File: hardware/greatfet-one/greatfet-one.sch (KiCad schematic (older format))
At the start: 98 parts, among them J1 NEIGHBOR1, J2 NEIGHBOR2, J3 USB-MICRO-B-SHIELDED, J4 USB-MICRO-B-SHIELDED, J5 JTAG, J6 POWER, J7 BONUS_ROW, SW1 DFU, SW2 RESET, U1 LPC4330FBD144, U2 W25Q16DV, U3 AP7333, U4 IP4220CZ6, U5 AP2553W6-7, X1 MCU_XTAL, X2 RTC_XTAL

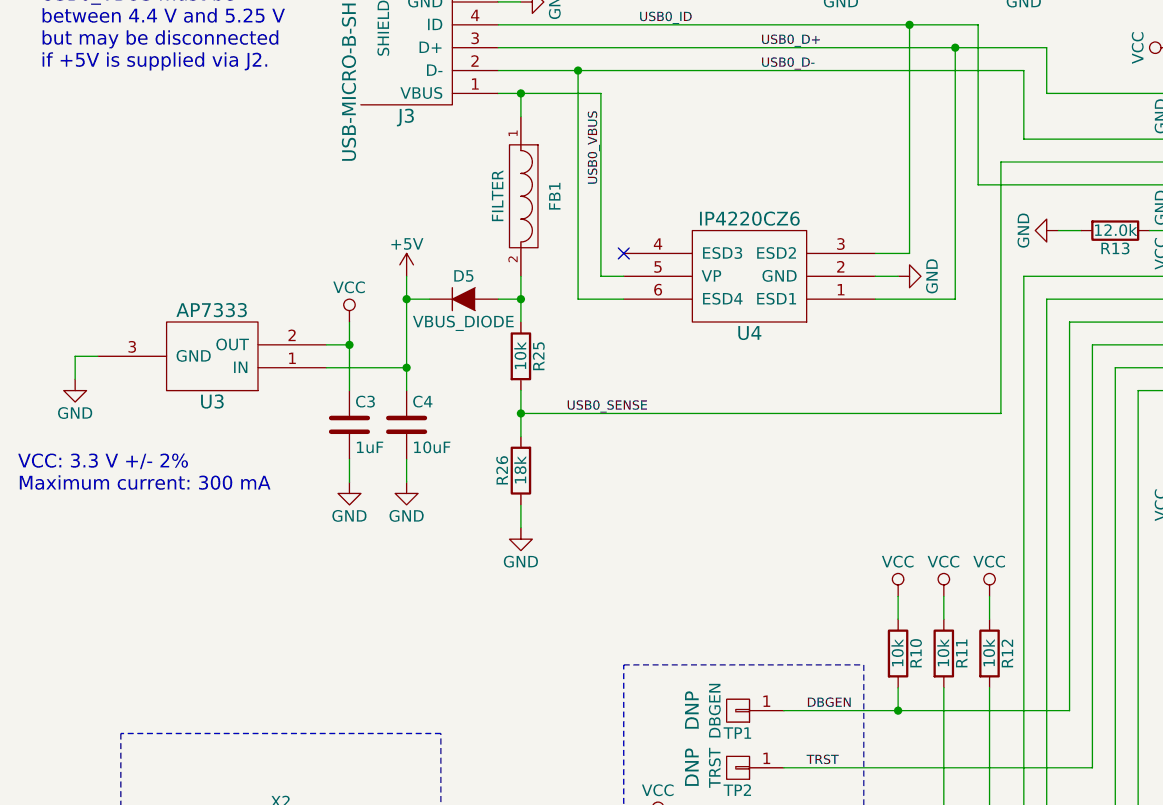
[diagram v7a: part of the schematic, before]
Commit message: GreatFET One: solder jumper to bypass VBUS diode
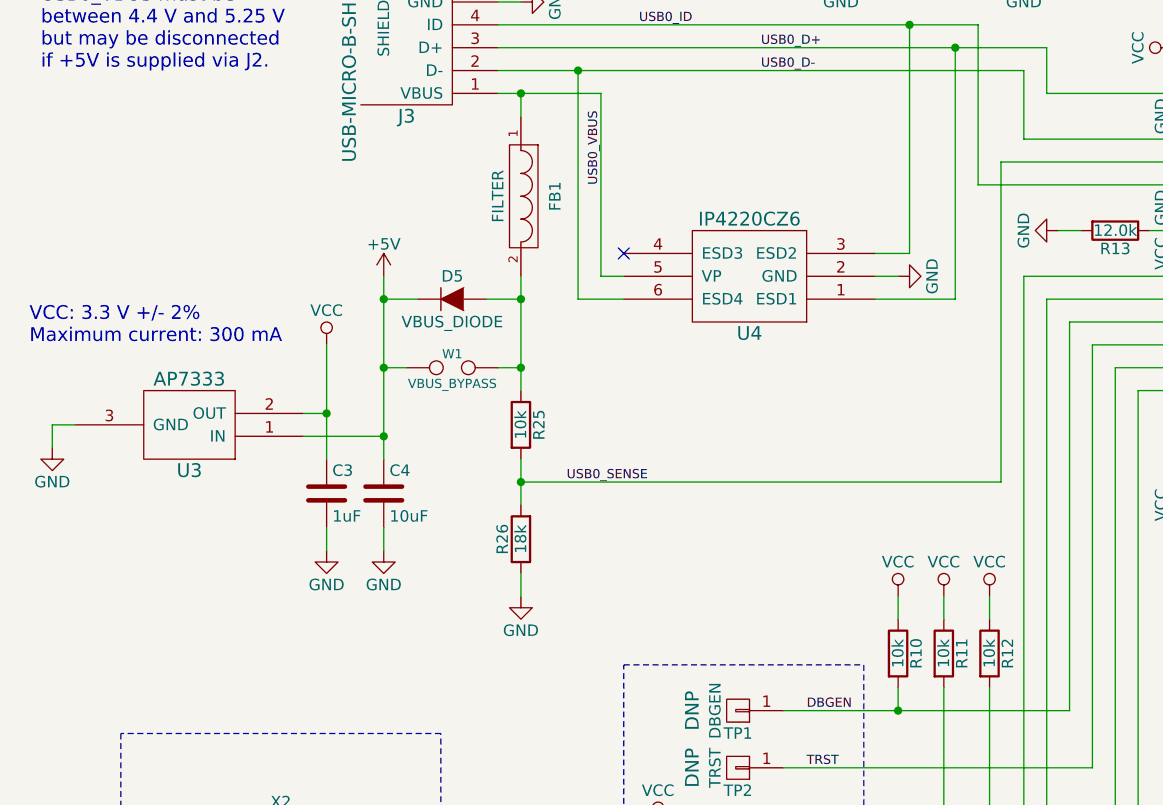
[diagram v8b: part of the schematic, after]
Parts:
- added W1: VBUS_BYPASS, gsg-modules:0603-JUMPER, symbol TEST
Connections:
- net +5V: now also W1.1
- net at D5.2 (A), FB1.2, R25.1: now also W1.2
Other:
- moved on the sheet: C3, C4, D5, R25, R26, U3
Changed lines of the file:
@@
 L AP7333 U3
 U 1 1 55E0B3C4
-P 1450 6450
-F 0 "U3" H 1450 6650 60  0000 C CNN
-F 1 "AP7333" H 1450 6250 60  0000 C CNN
-F 2 "gsg-modules:SOT23-3" H 1450 6450 60  0001 C CNN
-F 3 "" H 1450 6450 60  0000 C CNN
-F 4 "Diodes Inc." H 1450 6450 60  0001 C CNN "Manufacturer"
-F 5 "AP7333-33SAG-7" H 1450 6450 60  0001 C CNN "Part Number"
-F 6 "IC REG LDO 3.3V .3A SOT23" H 1450 6450 60  0001 C CNN "Description"
-	1    1450 6450
+P 1350 6750
+F 0 "U3" H 1350 6950 60  0000 C CNN
+F 1 "AP7333" H 1350 6550 60  0000 C CNN
+F 2 "gsg-modules:SOT23-3" H 1350 6750 60  0001 C CNN
+F 3 "" H 1350 6750 60  0000 C CNN
+F 4 "Diodes Inc." H 1350 6750 60  0001 C CNN "Manufacturer"
+F 5 "AP7333-33SAG-7" H 1350 6750 60  0001 C CNN "Part Number"
+F 6 "IC REG LDO 3.3V .3A SOT23" H 1350 6750 60  0001 C CNN "Description"
+	1    1350 6750
 	-1   0    0    1
 $EndComp
@@
 L C C4
 U 1 1 55E46B79
-P 2300 6750
-F 0 "C4" H 2325 6850 50  0000 L CNN
-F 1 "10uF" H 2325 6650 50  0000 L CNN
-F 2 "gsg-modules:0805" H 2338 6600 30  0001 C CNN
-F 3 "" H 2300 6750 60  0000 C CNN
-F 4 "Murata" H 2300 6750 60  0001 C CNN "Manufacturer"
-F 5 "GRM21BR61A106KE19L" H 2300 6750 60  0001 C CNN "Part Number"
-F 6 "CAP CER 10UF 10V 10% X5R 0805" H 2300 6750 60  0001 C CNN "Description"
-	1    2300 6750
+P 2200 7050
+F 0 "C4" H 2225 7150 50  0000 L CNN
+F 1 "10uF" H 2225 6950 50  0000 L CNN
+F 2 "gsg-modules:0805" H 2238 6900 30  0001 C CNN
+F 3 "" H 2200 7050 60  0000 C CNN
+F 4 "Murata" H 2200 7050 60  0001 C CNN "Manufacturer"
+F 5 "GRM21BR61A106KE19L" H 2200 7050 60  0001 C CNN "Part Number"
+F 6 "CAP CER 10UF 10V 10% X5R 0805" H 2200 7050 60  0001 C CNN "Description"
+	1    2200 7050
 	1    0    0    -1
 $EndComp
@@
 L C C3
 U 1 1 55E46D07
-P 2050 6750
-F 0 "C3" H 2075 6850 50  0000 L CNN
-F 1 "1uF" H 2075 6650 50  0000 L CNN
-F 2 "gsg-modules:0603" H 2088 6600 30  0001 C CNN
-F 3 "" H 2050 6750 60  0000 C CNN
-F 4 "Taiyo Yuden" H 2050 6750 60  0001 C CNN "Manufacturer"
-F 5 "LMK107B7105KA-T" H 2050 6750 60  0001 C CNN "Part Number"
-F 6 "CAP CER 1UF 10V 10% X7R 0603" H 2050 6750 60  0001 C CNN "Description"
-	1    2050 6750
+P 1950 7050
+F 0 "C3" H 1975 7150 50  0000 L CNN
+F 1 "1uF" H 1975 6950 50  0000 L CNN
+F 2 "gsg-modules:0603" H 1988 6900 30  0001 C CNN
+F 3 "" H 1950 7050 60  0000 C CNN
+F 4 "Taiyo Yuden" H 1950 7050 60  0001 C CNN "Manufacturer"
+F 5 "LMK107B7105KA-T" H 1950 7050 60  0001 C CNN "Part Number"
+F 6 "CAP CER 1UF 10V 10% X7R 0603" H 1950 7050 60  0001 C CNN "Description"
+	1    1950 7050
 	1    0    0    -1
 $EndComp
@@
 L VCC #PWR020
 U 1 1 55E4762F
-P 2050 6300
-F 0 "#PWR020" H 2050 6150 50  0001 C CNN
-F 1 "VCC" H 2050 6450 50  0000 C CNN
-F 2 "" H 2050 6300 60  0000 C CNN
-F 3 "" H 2050 6300 60  0000 C CNN
-	1    2050 6300
+P 1950 6400
+F 0 "#PWR020" H 1950 6250 50  0001 C CNN
+F 1 "VCC" H 1950 6550 50  0000 C CNN
+F 2 "" H 1950 6400 60  0000 C CNN
+F 3 "" H 1950 6400 60  0000 C CNN
+	1    1950 6400
 	1    0    0    -1
 $EndComp
@@
 L GND #PWR021
 U 1 1 55E47864
-P 2050 7000
-F 0 "#PWR021" H 2050 6750 50  0001 C CNN
-F 1 "GND" H 2050 6850 50  0000 C CNN
-F 2 "" H 2050 7000 60  0000 C CNN
-F 3 "" H 2050 7000 60  0000 C CNN
-	1    2050 7000
+P 1950 7300
+F 0 "#PWR021" H 1950 7050 50  0001 C CNN
+F 1 "GND" H 1950 7150 50  0000 C CNN
+F 2 "" H 1950 7300 60  0000 C CNN
+F 3 "" H 1950 7300 60  0000 C CNN
+	1    1950 7300
 	1    0    0    -1
 $EndComp
@@
 L GND #PWR022
 U 1 1 55E478D5
-P 2300 7000
-F 0 "#PWR022" H 2300 6750 50  0001 C CNN
-F 1 "GND" H 2300 6850 50  0000 C CNN
-F 2 "" H 2300 7000 60  0000 C CNN
-F 3 "" H 2300 7000 60  0000 C CNN
-	1    2300 7000
+P 2200 7300
+F 0 "#PWR022" H 2200 7050 50  0001 C CNN
+F 1 "GND" H 2200 7150 50  0000 C CNN
+F 2 "" H 2200 7300 60  0000 C CNN
+F 3 "" H 2200 7300 60  0000 C CNN
+	1    2200 7300
 	1    0    0    -1
 $EndComp
@@
 L GND #PWR023
 U 1 1 55E47A1E
-P 850 6550
-F 0 "#PWR023" H 850 6300 50  0001 C CNN
-F 1 "GND" H 850 6400 50  0000 C CNN
-F 2 "" H 850 6550 60  0000 C CNN
-F 3 "" H 850 6550 60  0000 C CNN
-	1    850  6550
+P 750 6850
+F 0 "#PWR023" H 750 6600 50  0001 C CNN
+F 1 "GND" H 750 6700 50  0000 C CNN
+F 2 "" H 750 6850 60  0000 C CNN
+F 3 "" H 750 6850 60  0000 C CNN
+	1    750  6850
 	1    0    0    -1
 $EndComp
@@
 Text Label 14050 6350 1    40   ~ 0
 USB1_SHIELD
-Text Notes 600  7050 0    60   ~ 0
+Text Notes 650  6400 0    60   ~ 0
 VCC: 3.3 V +/- 2%\nMaximum current: 300 mA
 $Comp
 L D D5
 U 1 1 57C0D534
-P 2550 6200
-F 0 "D5" H 2550 6300 50  0000 C CNN
-F 1 "VBUS_DIODE" H 2550 6100 50  0000 C CNN
-F 2 "gsg-modules:B140-13-F" H 2550 6200 60  0001 C CNN
-F 3 "" H 2550 6200 60  0000 C CNN
-F 4 "Diodes Inc." H 2550 6200 60  0001 C CNN "Manufacturer"
-F 5 "B140-13-F" H 2550 6200 60  0001 C CNN "Part Number"
-F 6 "DIODE SCHOTTKY 40V 1A SMA" H 2550 6200 60  0001 C CNN "Description"
-	1    2550 6200
+P 2500 6200
+F 0 "D5" H 2500 6300 50  0000 C CNN
+F 1 "VBUS_DIODE" H 2500 6100 50  0000 C CNN
+F 2 "gsg-modules:B140-13-F" H 2500 6200 60  0001 C CNN
+F 3 "" H 2500 6200 60  0000 C CNN
+F 4 "Diodes Inc." H 2500 6200 60  0001 C CNN "Manufacturer"
+F 5 "B140-13-F" H 2500 6200 60  0001 C CNN "Part Number"
+F 6 "DIODE SCHOTTKY 40V 1A SMA" H 2500 6200 60  0001 C CNN "Description"
+	1    2500 6200
 	1    0    0    -1
 $EndComp
@@
 L GND #PWR083
 U 1 1 57C0FA0A
-P 2800 7200
-F 0 "#PWR083" H 2800 6950 50  0001 C CNN
-F 1 "GND" H 2800 7050 50  0000 C CNN
-F 2 "" H 2800 7200 60  0000 C CNN
-F 3 "" H 2800 7200 60  0000 C CNN
-	1    2800 7200
+P 2800 7500
+F 0 "#PWR083" H 2800 7250 50  0001 C CNN
+F 1 "GND" H 2800 7350 50  0000 C CNN
+F 2 "" H 2800 7500 60  0000 C CNN
+F 3 "" H 2800 7500 60  0000 C CNN
+	1    2800 7500
 	1    0    0    -1
 $EndComp
@@
 L R R25
 U 1 1 57C0FA13
-P 2800 6450
-F 0 "R25" V 2880 6450 50  0000 C CNN
-F 1 "10k" V 2800 6450 50  0000 C CNN
-F 2 "gsg-modules:0603" V 2730 6450 30  0001 C CNN
-F 3 "" H 2800 6450 30  0000 C CNN
-F 4 "Panasonic" H 2800 6450 60  0001 C CNN "Manufacturer"
-F 5 "ERJ-3GEYJ103V" H 2800 6450 60  0001 C CNN "Part Number"
-F 6 "RES 10K OHM 1/10W 5% 0603 SMD" H 2800 6450 60  0001 C CNN "Description"
-	1    2800 6450
+P 2800 6750
+F 0 "R25" V 2880 6750 50  0000 C CNN
+F 1 "10k" V 2800 6750 50  0000 C CNN
+F 2 "gsg-modules:0603" V 2730 6750 30  0001 C CNN
+F 3 "" H 2800 6750 30  0000 C CNN
+F 4 "Panasonic" H 2800 6750 60  0001 C CNN "Manufacturer"
+F 5 "ERJ-3GEYJ103V" H 2800 6750 60  0001 C CNN "Part Number"
+F 6 "RES 10K OHM 1/10W 5% 0603 SMD" H 2800 6750 60  0001 C CNN "Description"
+	1    2800 6750
 	1    0    0    -1
 $EndComp
-Text Label 3000 6700 0    40   ~ 0
+Text Label 3000 7000 0    40   ~ 0
 USB0_SENSE
 $Comp
 L +5V #PWR084
 U 1 1 57C16251
-P 2300 6100
-F 0 "#PWR084" H 2300 5950 50  0001 C CNN
-F 1 "+5V" H 2300 6240 50  0000 C CNN
-F 2 "" H 2300 6100 60  0000 C CNN
-F 3 "" H 2300 6100 60  0000 C CNN
-	1    2300 6100
+P 2200 6100
+F 0 "#PWR084" H 2200 5950 50  0001 C CNN
+F 1 "+5V" H 2200 6240 50  0000 C CNN
+F 2 "" H 2200 6100 60  0000 C CNN
+F 3 "" H 2200 6100 60  0000 C CNN
+	1    2200 6100
 	1    0    0    -1
 $EndComp
@@
 L R R26
 U 1 1 57C512C9
-P 2800 6950
-F 0 "R26" V 2880 6950 50  0000 C CNN
-F 1 "18k" V 2800 6950 50  0000 C CNN
-F 2 "gsg-modules:0603" V 2730 6950 30  0001 C CNN
-F 3 "" H 2800 6950 30  0000 C CNN
-F 4 "Yageo" H 2800 6950 60  0001 C CNN "Manufacturer"
-F 5 "RC0603JR-0710KL" H 2800 6950 60  0001 C CNN "Part Number"
-F 6 "RES SMD 10K OHM 5% 1/10W 0603" H 2800 6950 60  0001 C CNN "Description"
-	1    2800 6950
+P 2800 7250
+F 0 "R26" V 2880 7250 50  0000 C CNN
+F 1 "18k" V 2800 7250 50  0000 C CNN
+F 2 "gsg-modules:0603" V 2730 7250 30  0001 C CNN
+F 3 "" H 2800 7250 30  0000 C CNN
+F 4 "Yageo" H 2800 7250 60  0001 C CNN "Manufacturer"
+F 5 "RC0603JR-0710KL" H 2800 7250 60  0001 C CNN "Part Number"
+F 6 "RES SMD 10K OHM 5% 1/10W 0603" H 2800 7250 60  0001 C CNN "Description"
+	1    2800 7250
 	-1   0    0    1
 $EndComp
@@
 	5750 6000 5850 6000
 Wire Wire Line
-	2300 6100 2300 6600
+	2200 6100 2200 6900
 Wire Wire Line
 	4900 5600 5850 5600
@@
 	3150 6100 3150 5300
 Wire Wire Line
-	1950 6400 2050 6400
+	1850 6700 1950 6700
 Wire Wire Line
-	2050 6300 2050 6600
-Connection ~ 2050 6400
+	1950 6400 1950 6900
+Connection ~ 1950 6700
 Wire Wire Line
-	2050 6900 2050 7000
+	1950 7200 1950 7300
 Wire Wire Line
-	2300 6900 2300 7000
+	2200 7200 2200 7300
 Wire Wire Line
-	850  6550 850  6450
+	750  6850 750  6750
 Wire Wire Line
-	850  6450 950  6450
+	750  6750 850  6750
 Wire Wire Line
 	11550 1650 11100 1650
@@
 	3050 6200 3050 5200
 Wire Wire Line
-	2800 7100 2800 7200
+	2800 7400 2800 7500
 Wire Wire Line
-	2800 6600 2800 6800
-Connection ~ 2800 6700
+	2800 6900 2800 7100
+Connection ~ 2800 7000
 Wire Wire Line
-	4900 6700 2800 6700
+	4900 7000 2800 7000
 Wire Wire Line
-	2800 6100 2800 6300
+	2800 6100 2800 6600
 Connection ~ 2800 6200
 Wire Wire Line
@@
 	2800 5300 2800 5400
 Connection ~ 2800 5300
-Connection ~ 2300 6200
+Connection ~ 2200 6200
 Wire Wire Line
 	12150 3100 12500 3100
 Wire Wire Line
-	2700 6200 2800 6200
+	2650 6200 2800 6200
 Wire Wire Line
-	1950 6500 2300 6500
-Connection ~ 2300 6500
+	1850 6800 2200 6800
+Connection ~ 2200 6800
 Wire Wire Line
-	2300 6200 2400 6200
+	2200 6200 2350 6200
 Wire Wire Line
-	4900 5600 4900 6700
+	4900 5600 4900 7000
 Wire Wire Line
 	10300 9850 10300 9500
@@
 Wire Wire Line
 	5750 1200 6100 1200
+$Comp
+L TEST W1
+U 1 1 57C655EF
+P 2500 6500
+F 0 "W1" H 2500 6560 40  0000 C CNN
+F 1 "VBUS_BYPASS" H 2500 6430 40  0000 C CNN
+F 2 "gsg-modules:0603-JUMPER" H 2500 6500 60  0001 C CNN
+F 3 "" H 2500 6500 60  0000 C CNN
+	1    2500 6500
+	1    0    0    -1
+$EndComp
+Wire Wire Line
+	2200 6500 2300 6500
+Connection ~ 2200 6500
+Wire Wire Line
+	2700 6500 2800 6500
+Connection ~ 2800 6500
 $EndSCHEMATC
